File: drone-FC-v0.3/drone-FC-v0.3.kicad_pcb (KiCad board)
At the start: 2 copper layers, 6 parts, among them U1 MCP1727-3302xSN, U2 ESP32-S3-WROOM-1

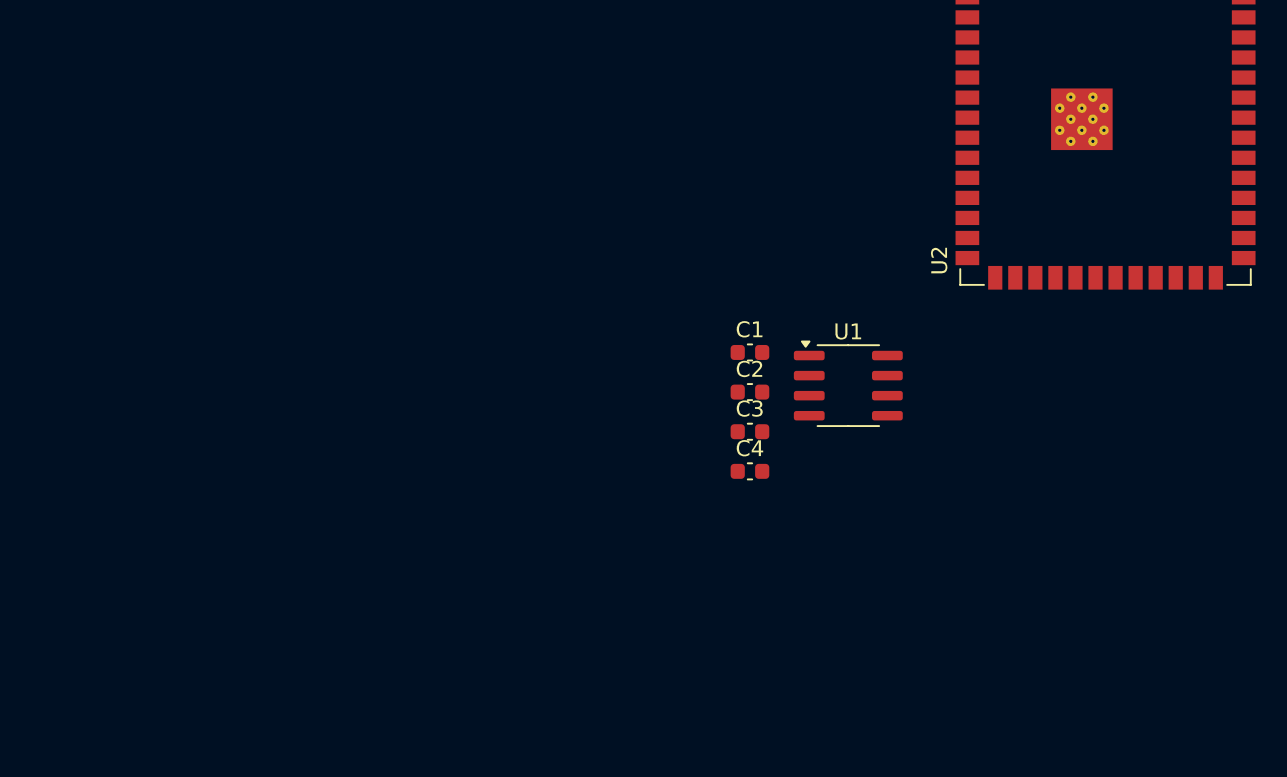
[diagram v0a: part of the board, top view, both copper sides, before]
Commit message: what
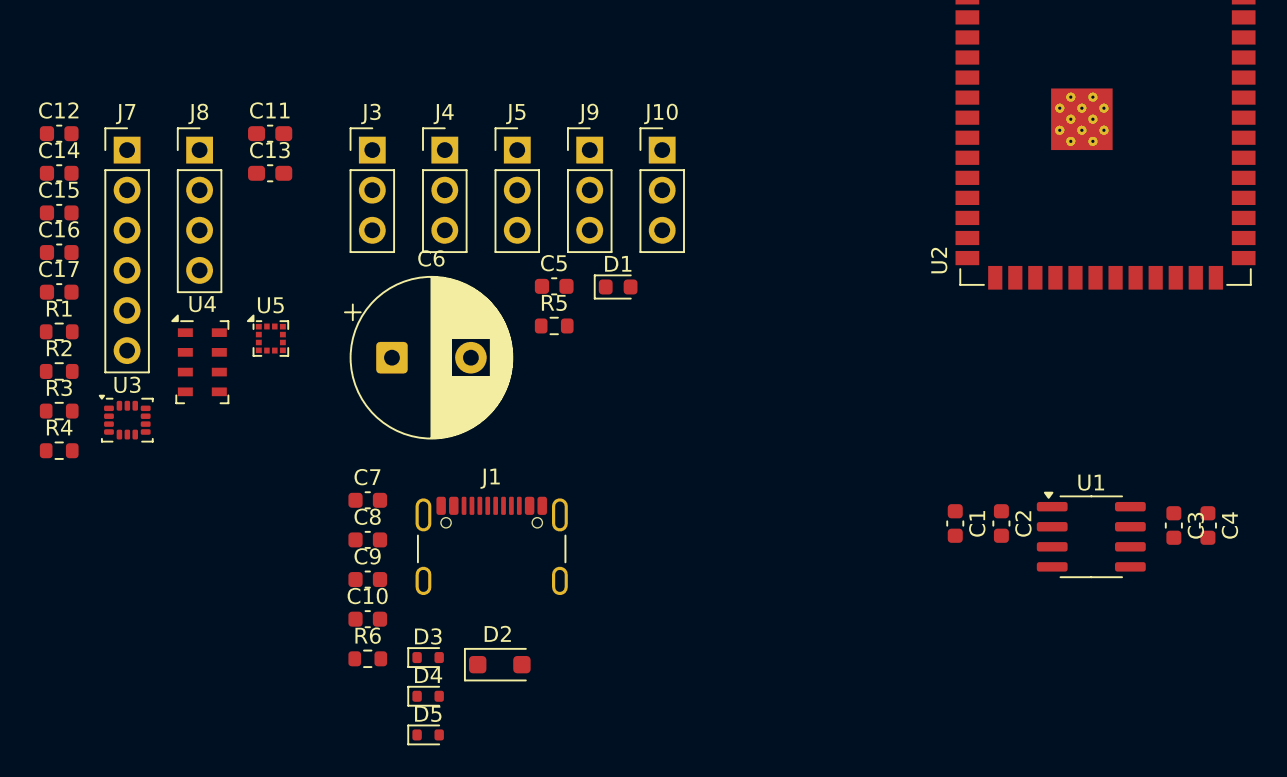
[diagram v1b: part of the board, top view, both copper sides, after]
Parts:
- added C10: 1uF/16v, Capacitor_SMD:C_0603_1608Metric, F.Cu at (115.6, 120.7)
- added C11: 0.1uF, Capacitor_SMD:C_0603_1608Metric_Pad1.08x0.95mm_HandSolder, F.Cu at (109.4, 89.9)
- added C12: 4.7uF, Capacitor_SMD:C_0603_1608Metric, F.Cu at (96.1, 89.9)
- added C13: 0.1uF, Capacitor_SMD:C_0603_1608Metric_Pad1.08x0.95mm_HandSolder, F.Cu at (109.4, 92.4)
- added C14: 0.1uF, Capacitor_SMD:C_0603_1608Metric, F.Cu at (96.1, 92.4)
- added C15: 1uF, Capacitor_SMD:C_0603_1608Metric, F.Cu at (96.1, 94.9)
- added C16: 0.1uF, Capacitor_SMD:C_0603_1608Metric, F.Cu at (96.1, 97.4)
- added C17: 0.1uF, Capacitor_SMD:C_0603_1608Metric, F.Cu at (96.1, 100.0)
- added C5: 0.1uF, Capacitor_SMD:C_0603_1608Metric, F.Cu at (127.4, 99.6)
- added C6: 470uF, Capacitor_THT:CP_Radial_D10.0mm_P5.00mm, F.Cu at (117.1, 104.1)
- added C7: 10uF/25V, Capacitor_SMD:C_0603_1608Metric, F.Cu at (115.6, 113.1)
- added C8: 10uF, Capacitor_SMD:C_0603_1608Metric, F.Cu at (115.6, 115.6)
- added C9: 0.1uF, Capacitor_SMD:C_0603_1608Metric, F.Cu at (115.6, 118.2)
- added D1: 1V8, LED_SMD:LED_0603_1608Metric, F.Cu at (131.5, 99.6)
- added D2: D, Diode_SMD:D_SOD-123F, F.Cu at (124.0, 123.5)
- added D3: D, Diode_SMD:D_SOD-523, F.Cu at (119.4, 123.1)
- added D4: D, Diode_SMD:D_SOD-523, F.Cu at (119.4, 125.5)
- added D5: D, Diode_SMD:D_SOD-523, F.Cu at (119.4, 128.0)
- added J1: USB_C_Receptacle_USB2.0_16P, Connector_USB:USB_C_Receptacle_GCT_USB4105-xx-A_16P_TopMnt_Horizontal, F.Cu at (123.4, 117.2)
- added J10: S5, Connector_PinHeader_2.54mm:PinHeader_1x03_P2.54mm_Vertical, F.Cu at (134.2, 91.0)
- added J3: S2, Connector_PinHeader_2.54mm:PinHeader_1x03_P2.54mm_Vertical, F.Cu at (115.9, 91.0)
- added J4: S3, Connector_PinHeader_2.54mm:PinHeader_1x03_P2.54mm_Vertical, F.Cu at (120.5, 91.0)
- added J5: S1, Connector_PinHeader_2.54mm:PinHeader_1x03_P2.54mm_Vertical, F.Cu at (125.1, 91.0)
- added J7: ICM, Connector_PinHeader_2.54mm:PinHeader_1x06_P2.54mm_Vertical, F.Cu at (100.4, 91.0)
- added J8: UART0, Connector_PinHeader_2.54mm:PinHeader_1x04_P2.54mm_Vertical, F.Cu at (104.9, 91.0)
- added J9: S4, Connector_PinHeader_2.54mm:PinHeader_1x03_P2.54mm_Vertical, F.Cu at (129.7, 91.0)
- added R1: 4.7k, Resistor_SMD:R_0603_1608Metric, F.Cu at (96.1, 102.5)
- added R2: 4.7k, Resistor_SMD:R_0603_1608Metric, F.Cu at (96.1, 105.0)
- added R3: 4.7k, Resistor_SMD:R_0603_1608Metric, F.Cu at (96.1, 107.5)
- added R4: 4.7k, Resistor_SMD:R_0603_1608Metric, F.Cu at (96.1, 110.0)
- added R5: 100, Resistor_SMD:R_0603_1608Metric, F.Cu at (127.4, 102.1)
- added R6: 10k, Resistor_SMD:R_0603_1608Metric, F.Cu at (115.6, 123.2)
- added U3: LSM6DSOX, Package_LGA:LGA-14_3x2.5mm_P0.5mm_LayoutBorder3x4y, F.Cu at (100.4, 108.1)
- added U4: MS5607-02BA, Package_LGA:LGA-8_3x5mm_P1.25mm, F.Cu at (105.1, 104.4)
- added U5: LIS3MDL, Package_LGA:LGA-12_2x2mm_P0.5mm, F.Cu at (109.5, 102.9)
- C3: value C -> 0.1uF
- C4: value C -> 10uF
- moved C4 29.2 mm to (168.8, 114.7), turned to -90 degrees
- moved C3 27.5 mm to (166.6, 114.7), turned to -90 degrees
- moved U1 18.1 mm to (161.4, 115.4)
- moved C2 18.0 mm to (155.7, 114.6), turned to -90 degrees
- moved C1 16.9 mm to (152.8, 114.6), turned to -90 degrees
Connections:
- U2 pad 10: unconnected-(U2-IO17-Pad10) -> /MCU/UART_1_TX
- U2 pad 11: unconnected-(U2-IO18-Pad11) -> /MCU/UART_1_RX
- U2 pad 12: unconnected-(U2-IO8-Pad12) -> /MCU/GPIO8
- U2 pad 13: unconnected-(U2-USB_D--Pad13) -> /MCU/USB_D-
- U2 pad 14: unconnected-(U2-USB_D+-Pad14) -> /MCU/USB_D+
- U2 pad 3: unconnected-(U2-EN-Pad3) -> /MCU/CHIP_PU
- U2 pad 36: unconnected-(U2-RXD0-Pad36) -> /MCU/UART_0_RX
- U2 pad 37: unconnected-(U2-TXD0-Pad37) -> /MCU/UART_0_TX
- U2 pad 4: unconnected-(U2-IO4-Pad4) -> /MCU/GPIO4
- U2 pad 5: unconnected-(U2-IO5-Pad5) -> /MCU/GPIO5
- U2 pad 6: unconnected-(U2-IO6-Pad6) -> /MCU/GPIO6
- U2 pad 7: unconnected-(U2-IO7-Pad7) -> /MCU/GPIO7

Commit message: whatever
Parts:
- added C18: 100nF, Capacitor_SMD:C_0402_1005Metric, F.Cu at (206.7, 104.0)
- added C19: 100nF, Capacitor_SMD:C_0402_1005Metric, F.Cu at (206.7, 106.0)
- added C20: C, Capacitor_SMD:C_0201_0603Metric, F.Cu at (206.5, 107.9)
- added C21: 100nF, Capacitor_SMD:C_0603_1608Metric_Pad1.08x0.95mm_HandSolder, F.Cu at (194.3, 96.3)
- added C22: C, Capacitor_SMD:C_0603_1608Metric_Pad1.08x0.95mm_HandSolder, F.Cu at (194.3, 98.8)
- added C23: 10 uF, Capacitor_SMD:C_0201_0603Metric, F.Cu at (192.3, 127.6)
- added C6: something idk yet, Capacitor_THT:C_Radial_D6.3mm_H5.0mm_P2.50mm, F.Cu at (206.9, 119.8)
- added D6: ESD9B3.3ST5G, Diode_SMD:D_SOD-923, F.Cu at (200.9, 116.9)
- added D7: ESD9B3.3ST5G, Diode_SMD:D_SOD-923, F.Cu at (200.9, 118.8)
- added D8: 1N4148WT, Diode_SMD:D_SOD-523, F.Cu at (189.3, 127.9)
- added D9: ESD9B3.3ST5G, Diode_SMD:D_SOD-923, F.Cu at (200.9, 120.8)
- added J11: USB_C_Receptacle_USB2.0_16P, Connector_USB:USB_C_Receptacle_Amphenol_124019772112A, F.Cu at (193.5, 121.3)
- added J2: Conn_01x04_Pin, Connector:FanPinHeader_1x04_P2.54mm_Vertical, F.Cu at (198.7, 98.7)
- added J6: Conn_01x04_Pin, Connector_PinSocket_2.00mm:PinSocket_1x04_P2.00mm_Vertical, F.Cu at (198.5, 105.1)
- added R10: 10k, Resistor_SMD:R_0603_1608Metric_Pad0.98x0.95mm_HandSolder, F.Cu at (194.3, 103.8)
- added R11: 10kohm, Resistor_SMD:R_0603_1608Metric_Pad0.98x0.95mm_HandSolder, F.Cu at (194.3, 106.3)
- added R12: 10kohm, Resistor_SMD:R_0603_1608Metric_Pad0.98x0.95mm_HandSolder, F.Cu at (194.3, 108.8)
- added R7: 4.7k, Resistor_SMD:R_0402_1005Metric, F.Cu at (206.8, 110.8)
- added R8: 4.7k, Resistor_SMD:R_0402_1005Metric, F.Cu at (206.8, 112.8)
- added R9: 10k, Resistor_SMD:R_0603_1608Metric_Pad0.98x0.95mm_HandSolder, F.Cu at (194.3, 101.3)
- added U6: LIS3MDL, Package_LGA:LGA-12_2x2mm_P0.5mm, F.Cu at (194.1, 112.1)
- added U7: MS5607-02BA, Package_LGA:LGA-8_3x5mm_P1.25mm, F.Cu at (203.0, 106.6)
- added U8: LSM6DSOX, Package_LGA:LGA-14_3x2.5mm_P0.5mm_LayoutBorder3x4y, F.Cu at (203.1, 111.9)
- added connector1: Conn_01x06_Pin, Connector_PinHeader_2.54mm:PinHeader_1x06_P2.54mm_Vertical, F.Cu at (189.8, 97.3)
- J10: value S5 -> M1

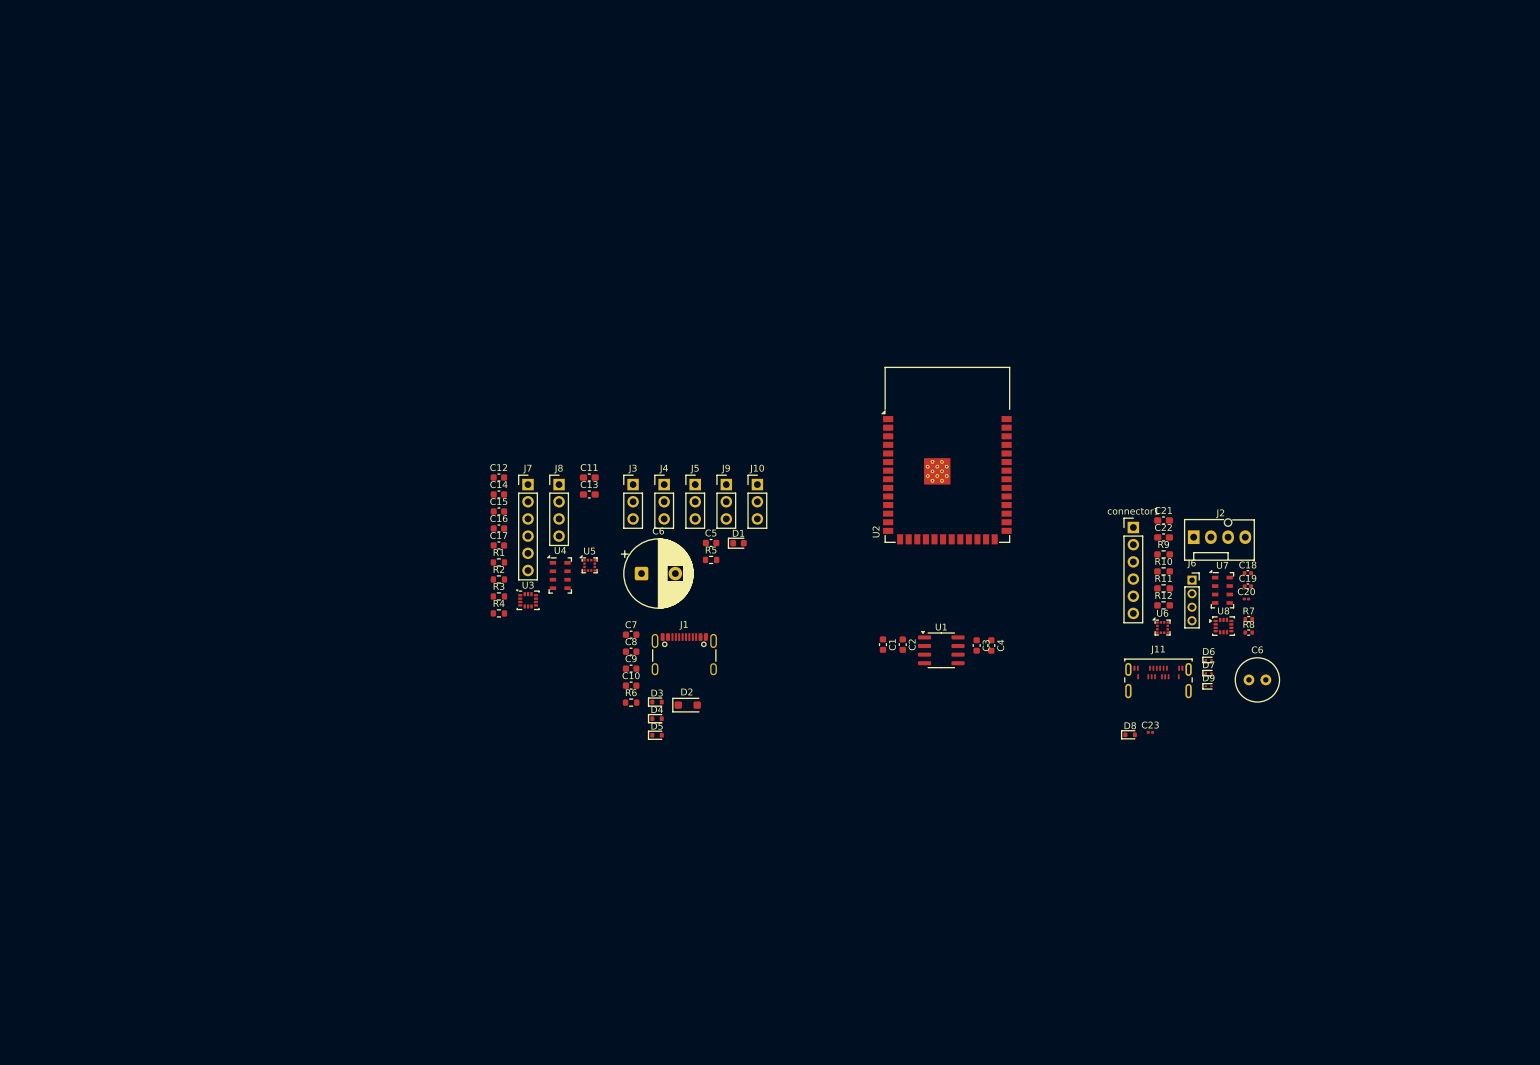
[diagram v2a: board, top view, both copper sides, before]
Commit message: modified the schematics to three sensors and added some of the PCB layouts
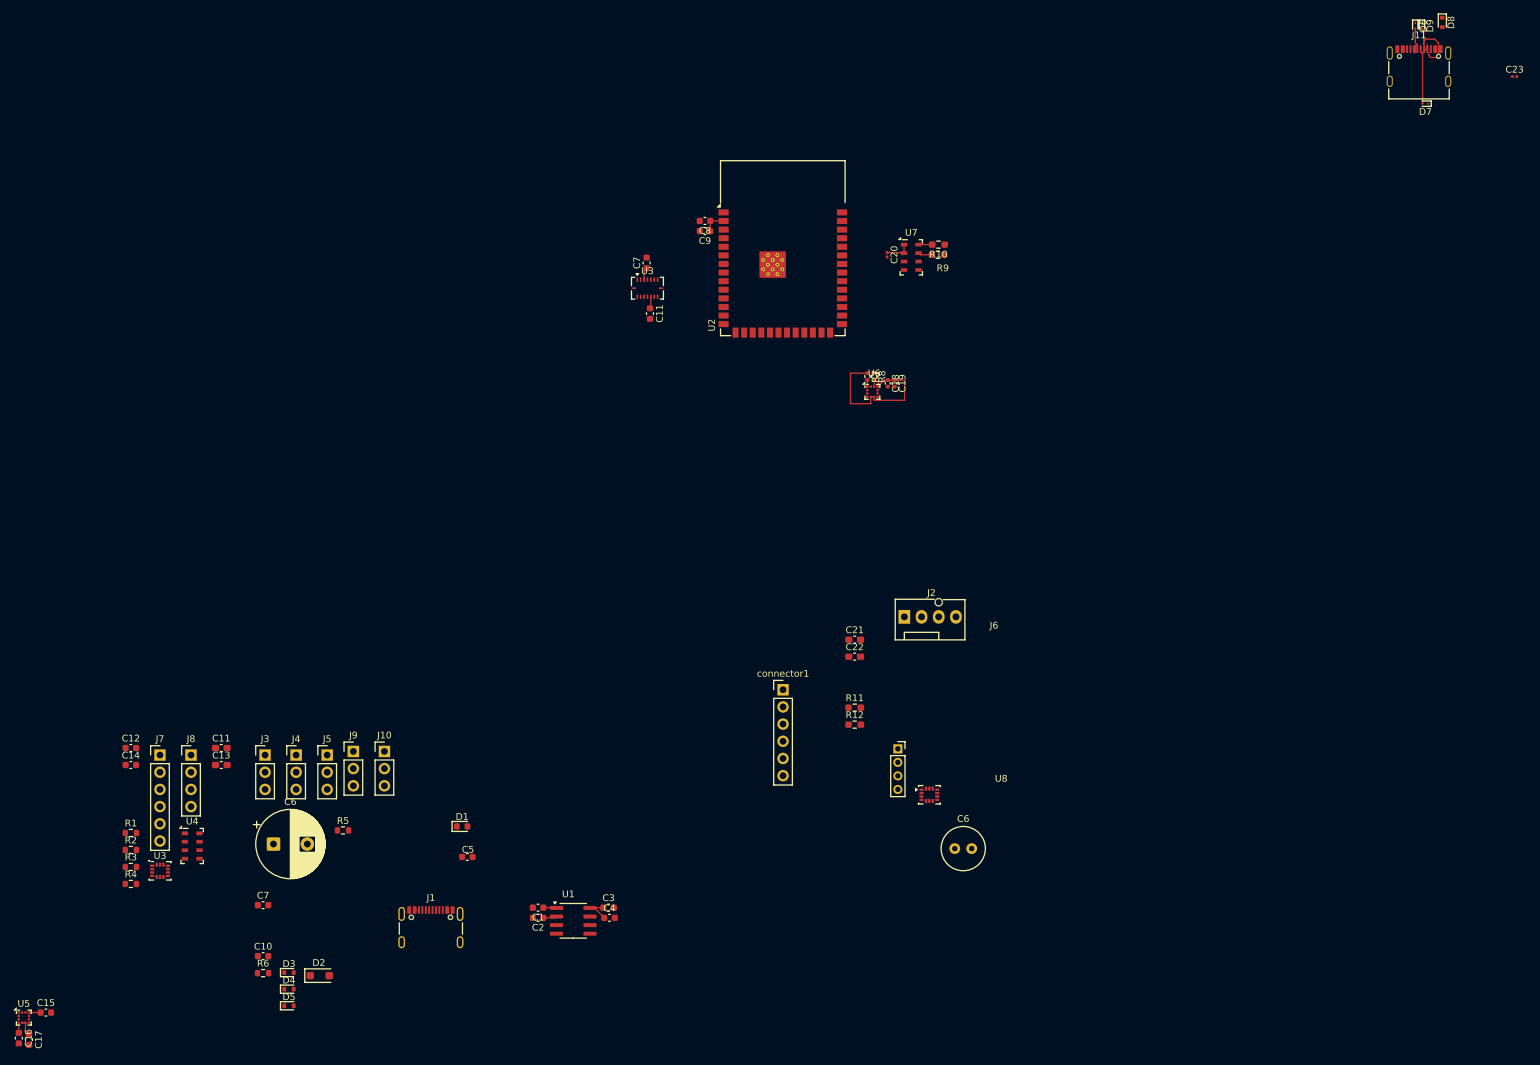
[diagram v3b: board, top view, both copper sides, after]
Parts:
- added C11: 100nF, Capacitor_SMD:C_0603_1608Metric, F.Cu at (118.4, 65.7)
- added C7: 100nF, Capacitor_SMD:C_0603_1608Metric, F.Cu at (117.9, 58.2)
- added U3: BMI088, Package_LGA:Bosch_LGA-16_4.5x3mm_P0.5mm_LayoutBorder7x1y_ClockwisePinNumbering, F.Cu at (118.0, 61.9)
- J11: footprint Connector_USB:USB_C_Receptacle_Amphenol_124019772112A -> Connector_USB:USB_C_Receptacle_Palconn_UTC16-G
- moved D8 114.9 mm to (235.4, 22.7), turned to -90 degrees
- moved C23 110.8 mm to (246.1, 30.7)
- moved U5 107.0 mm to (25.9, 169.7)
- moved C16 103.4 mm to (25.1, 172.7), turned to -90 degrees
- moved D9 102.6 mm to (232.4, 23.2), turned to -90 degrees
- moved C17 100.8 mm to (26.6, 173.0), turned to -90 degrees
- moved J11 99.9 mm to (232.0, 29.1)
- moved C15 99.8 mm to (29.1, 169.0)
- moved D6 98.5 mm to (231.4, 23.2), turned to -90 degrees
- moved D7 90.0 mm to (232.9, 34.7), turned to 180 degrees
- moved C20 73.5 mm to (153.4, 57.0), turned to -90 degrees
- moved C4 69.3 mm to (112.4, 155.0), turned to 0 degrees
- moved J10 67.8 mm to (79.1, 130.4)
- moved J9 67.8 mm to (74.5, 130.4)
- moved C11 67.5 mm to (55.0, 129.9)
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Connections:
- net /Sensors/sclk_1 renamed /Sensors/SCLK
- R9 pad 2: /Sensors/sda_1 -> /Sensors/GPIO8
- U2 pad 15: unconnected-(U2-IO3-Pad15) -> /MCU/SCLK
- U2 pad 17: unconnected-(U2-IO9-Pad17) -> /MCU/Low_chip_selected
- U2 pad 18: unconnected-(U2-IO10-Pad18) -> /MCU/SCL_MAG
- U2 pad 19: unconnected-(U2-IO11-Pad19) -> /MCU/SDA_MAG
- U2 pad 30: unconnected-(U2-IO37-Pad30) -> /MCU/SDO1
- U7 pad 6: /Sensors/sdo_1 -> unconnected-(U7-SDO-Pad6)
- U7 pad 7: /Sensors/sda_1 -> /Sensors/GPIO8
- connector1 pad 2: /Sensors/sdo_1 -> /Sensors/SDO1
- connector1 pad 3: /Sensors/sda_1 -> unconnected-(connector1-Pin_3-Pad3)
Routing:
- net +3V3: track 0.00 -> 38.8 mm
- net /MCU/GPIO 20: track 0.00 -> 9.39 mm
- net /MCU/GPIO 19: track 0.00 -> 9.13 mm
- net VDD: track 0.00 -> 5.65 mm
- net +5V: track 0.00 -> 3.98 mm
- net Net-(D6-A2): track 0.00 -> 3.79 mm
- net /Sensors/GPIO8: track 0.00 -> 2.04 mm
- net /Sensors/SCLK: track 0.00 -> 2.03 mm
- net +3.3V: track 0.00 -> 1.76 mm
- net Net-(U5-C1): track 0.00 -> 1.51 mm
- net /Sensors/SCL_MAG: track 0.00 -> 1.01 mm
- net /Sensors/SDA_MAG: track 0.00 -> 0.98 mm

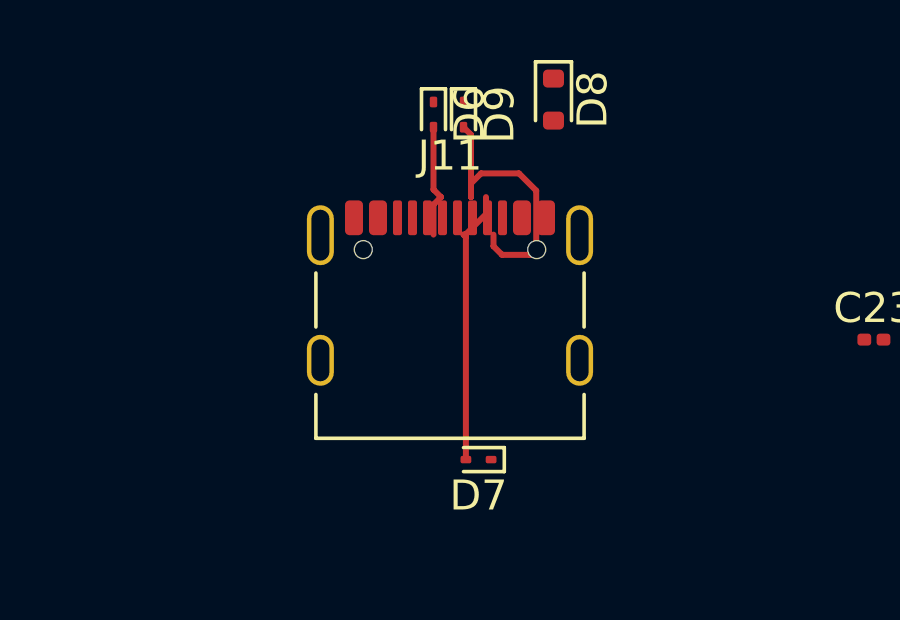
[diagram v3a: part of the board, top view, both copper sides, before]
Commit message: fixed usb footprint issue
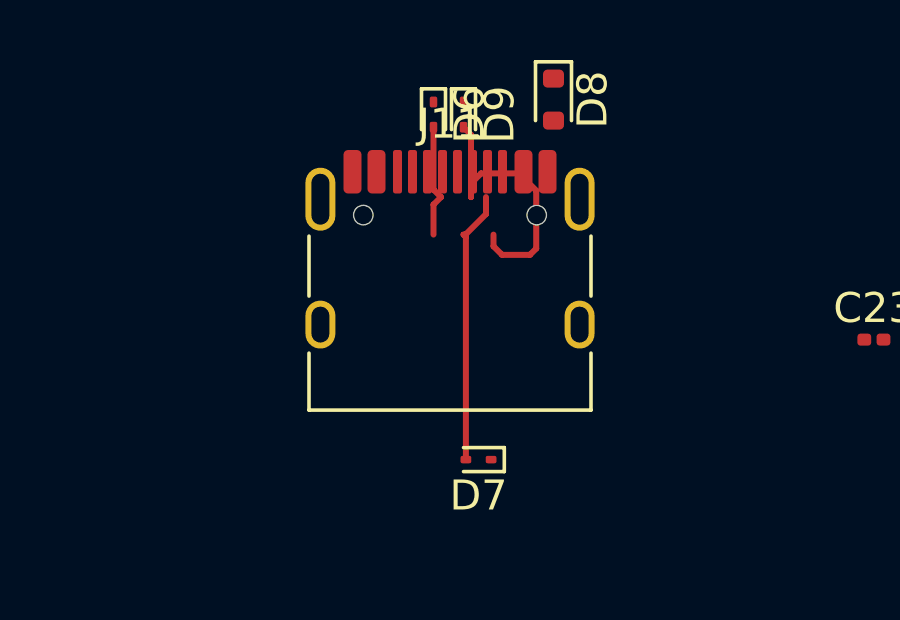
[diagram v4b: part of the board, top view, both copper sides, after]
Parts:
- J11: footprint Connector_USB:USB_C_Receptacle_Palconn_UTC16-G -> Connector_USB:USB_C_Receptacle_HRO_TYPE-C-31-M-12
